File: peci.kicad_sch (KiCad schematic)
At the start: 16 parts, among them Q2 PJE138K, U30 MAX6621AUBT, U31 NTS0104_DHVQFN, U32 FXMAR2104UMX

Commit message: [#83609] Reannotate board
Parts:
- renumbered C146 to C166, C144 to C167, C152 to C168, C148 to C169, C151 to C170, C153 to C171, Q2 to Q4, R197 to R288, R200 to R289, R198 to R290, R199 to R291, R201 to R292, TP2 to TP24, U32 to U35, U30 to U36, U31 to U37

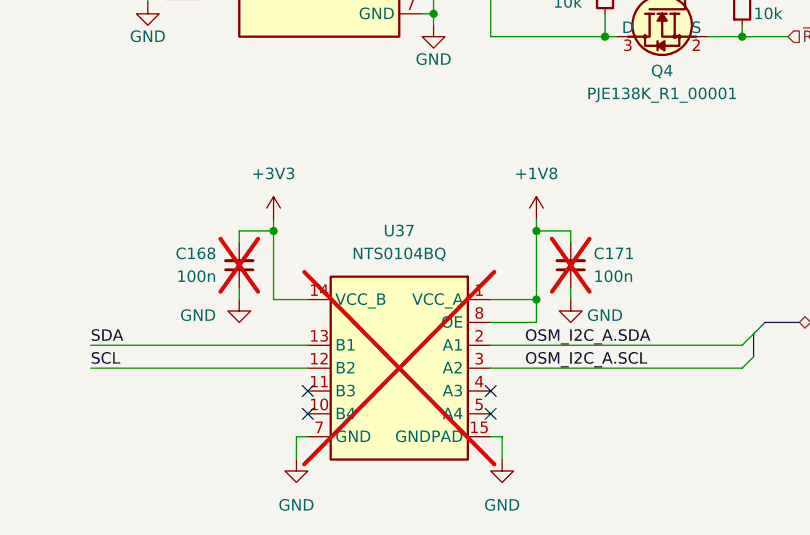
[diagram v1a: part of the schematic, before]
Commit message: [#83904] Add level shifters, clear ERC
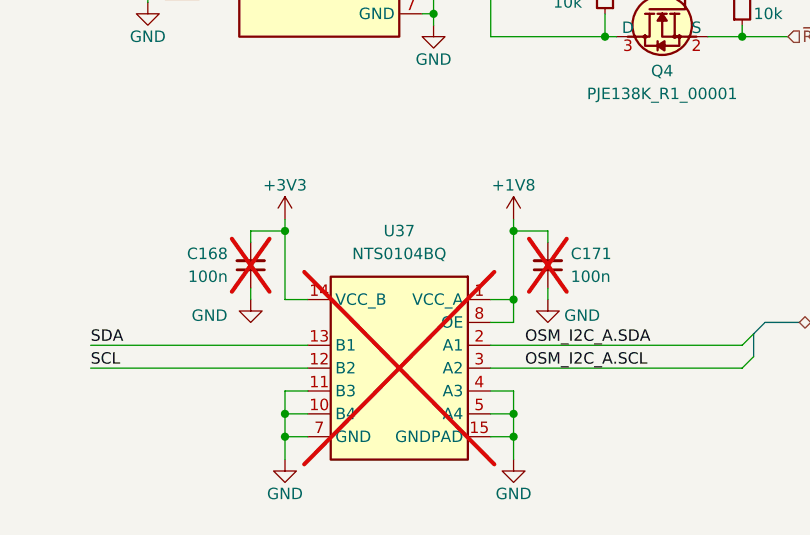
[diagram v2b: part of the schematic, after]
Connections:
- net GND: now also U37.10 (B4), U37.11 (B3), U37.4 (A3), U37.5 (A4)
- no-connect marks 10 -> 6
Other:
- moved on the sheet: C168, C171
